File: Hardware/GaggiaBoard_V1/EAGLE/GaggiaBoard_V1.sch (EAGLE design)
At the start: 122 parts, among them IC1 LD117ADT33TR, J10 PIN262409-1, J11 PIN262409-1, J12 PIN262409-1, J13 PIN262409-1, J14 PIN262409-1, J15 PIN262409-1, J16 PIN262409-1, J17 PIN262409-1, J18 PIN262409-1, J19 PIN262409-1, J2 QWIIC_RIGHT_ANGLE, J20 PIN262409-1, J21 PIN262409-1, J22 PIN262409-1, J23 PIN262409-1, J24 5033981892, J3 QWIIC_RIGHT_ANGLE, J4 1X2-3.5MM, J5 1X2-3.5MM, K1 RELAY-SPDT-JZC-11F, K2 RELAY-SPDT-JZC-11F, K3 RELAY-SPDT-JZC-11F, Q1 600mA/40V, Q2 600mA/40V, Q3 600mA/40V, Q4 600mA/40V, Q5 600mA/40V, Q6 600mA/40V, Q8 600mA/40V, Q9 600mA/40V, U1 BLACKPILL, U2 MAX31855K, U3 MAX31855K

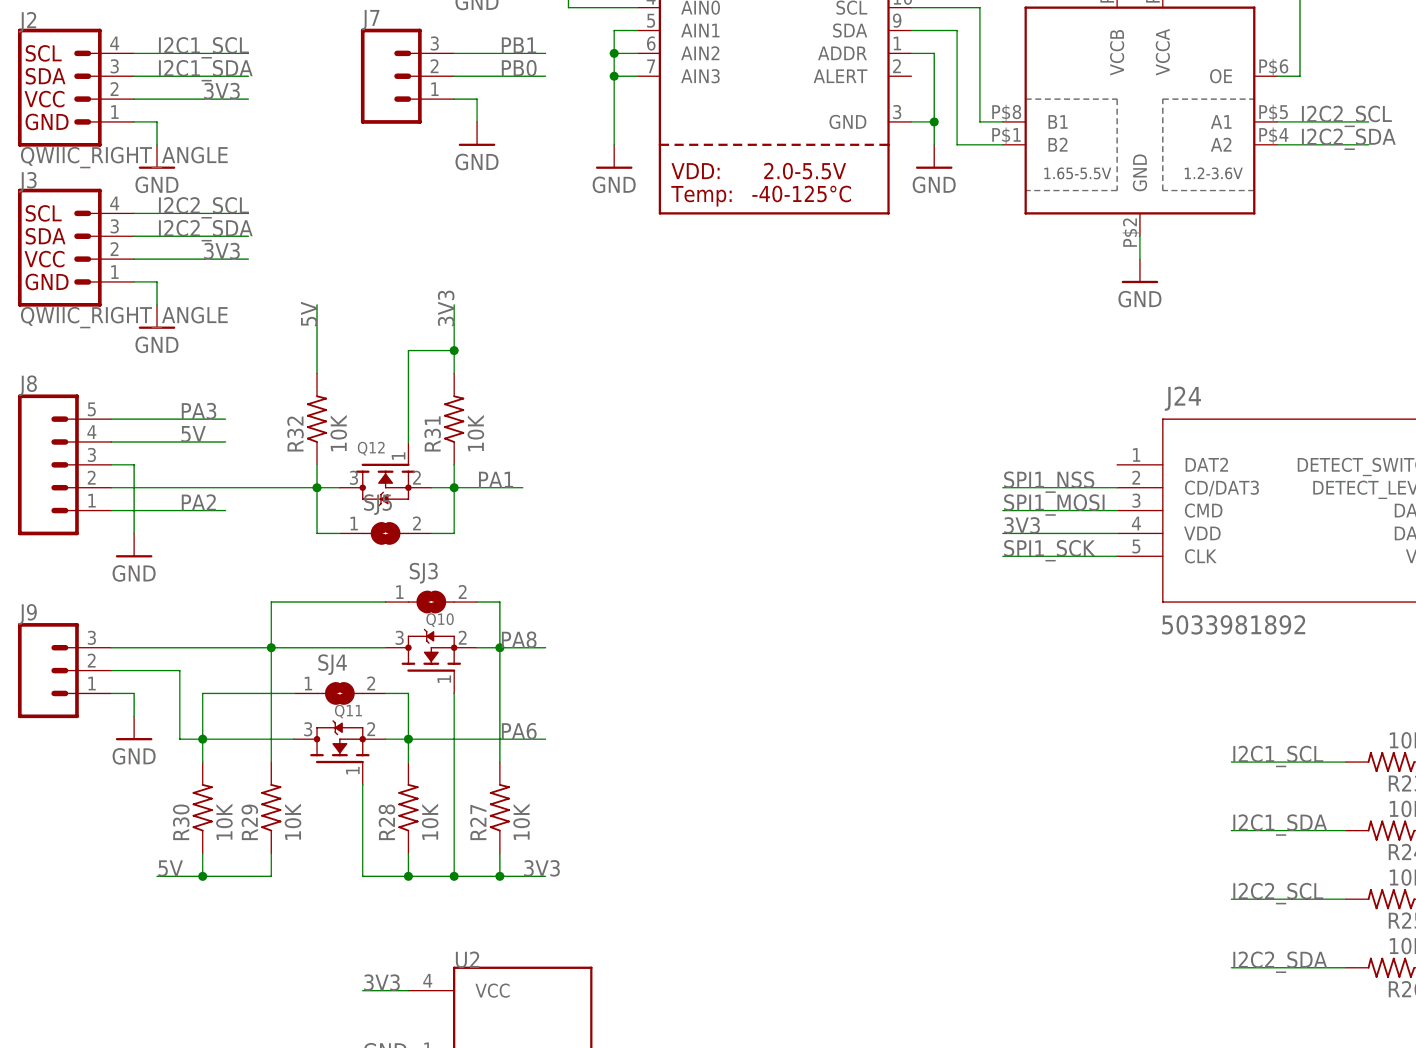
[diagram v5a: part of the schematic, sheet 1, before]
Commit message: TXU0102 level shifter for SSRs
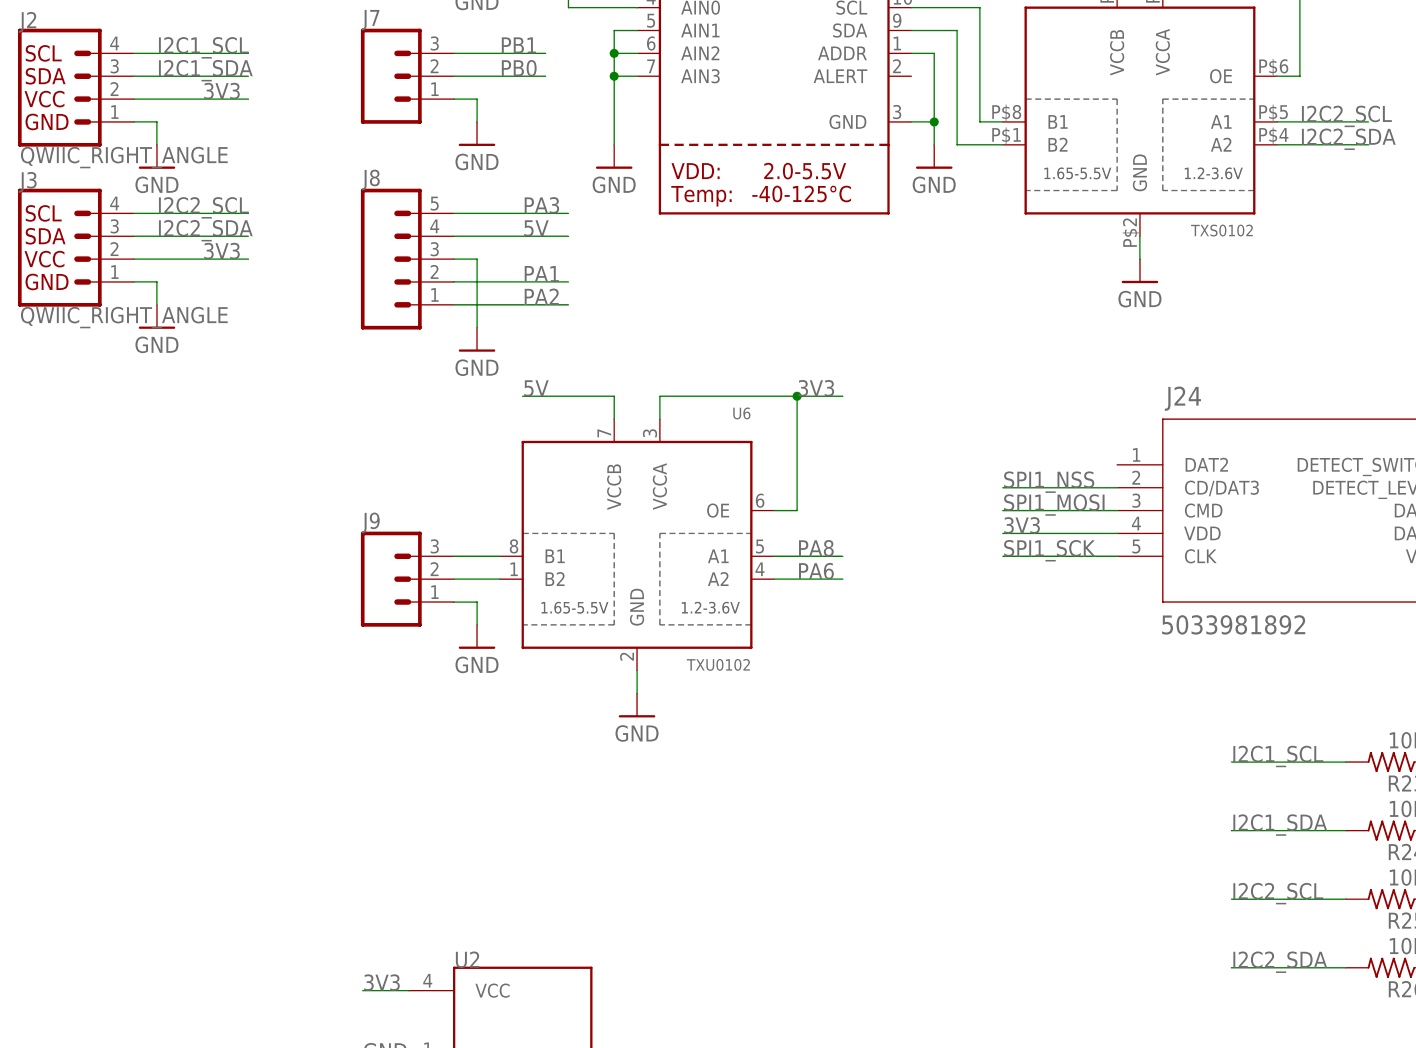
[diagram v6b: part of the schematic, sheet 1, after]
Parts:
- removed Q10, Q11, Q12: (no value), microbuilder:MOSFET-NREFLOW
- removed R27, R28, R29, R30, R31, R32: 10K, rcl:R-US_R0603
- removed SJ3, SJ4, SJ5: (no value), microbuilder:SOLDERJUMPER
- added U6: TXU0102, microbuilder:TXS0102
- U5: value (none) -> TXS0102
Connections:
- removed net N$43: J8.2, Q12.D, R32.1, SJ5.1
- net 3V3: now also U6.OE, U6.VCCA; no longer Q10.G, Q11.G, Q12.G, R27.1, R28.1, R31.2
- net 5V: now also U6.VCCB; no longer R29.1, R30.1, R32.2
- net GND: now also U6.GND
- net N$41: now also J9.3, U6.B1; no longer J9.2, Q11.D, R30.2, SJ4.1
- net N$42: now also J9.2, U6.B2; no longer J9.3, Q10.D, R29.2, SJ3.1
- net PA1: now also J8.2; no longer Q12.S, R31.1, SJ5.2
- net PA6: now also U6.A2; no longer Q11.S, R28.2, SJ4.2
- net PA8: now also U6.A1; no longer Q10.S, R27.2, SJ3.2
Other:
- moved on the sheet: J8, J9

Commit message: UARTs reassigned, LEDs fixed
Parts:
- added J27: (no value), SparkFun-Connectors:CONN_041X04_NO_SILK
- LED1, LED2, LED3, LED4: device led:LEDCHIP-LED0603 -> adafruit:LEDCHIPLED_1206
- R6: value 10k -> 10K
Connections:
- net UART1_5V_RX renamed UART6_5V_RX
- net UART1_5V_TX renamed UART6_5V_TX
- new net UART6_RX: Q7G$2.S, R18.1, SJ2.1, U1.PA12
- new net UART6_TX: Q7G$1.S, R19.1, SJ1.1, U1.PA11
- net 3V3: now also J27.1
- net GND: now also J27.4
- net UART1_RX: now also J27.3; no longer Q7G$2.S, R18.1, SJ2.1
- net UART1_TX: now also J27.2; no longer Q7G$1.S, R19.1, SJ1.1

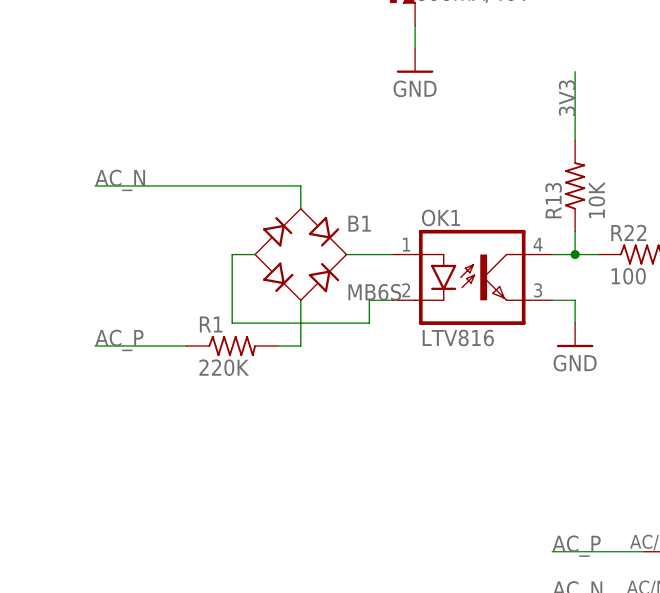
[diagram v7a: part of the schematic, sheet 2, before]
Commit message: Connectors spacing fixed
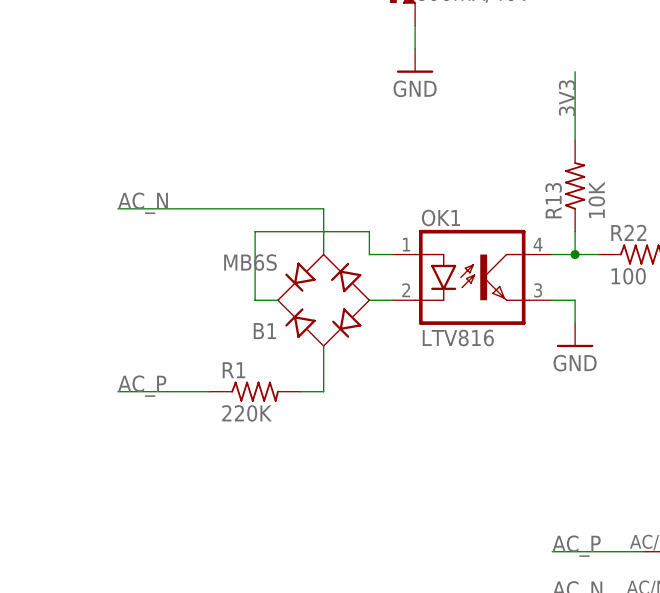
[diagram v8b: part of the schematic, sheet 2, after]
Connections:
- net AC_N: now also B1.AC2; no longer B1.AC1
- net N$37: now also B1.AC1; no longer B1.AC2
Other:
- moved on the sheet: B1, R1
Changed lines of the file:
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@@
 <attribute name="LCSC" x="50.8" y="68.58" size="1.778" layer="96" display="off"/>
 </instance>
-<instance part="R1" gate="G$1" x="22.86" y="60.96" smashed="yes">
-<attribute name="NAME" x="19.05" y="62.4586" size="1.778" layer="95"/>
-<attribute name="VALUE" x="19.05" y="57.658" size="1.778" layer="96"/>
-<attribute name="LCSC" x="22.86" y="60.96" size="1.778" layer="96" display="off"/>
+<instance part="R1" gate="G$1" x="25.4" y="55.88" smashed="yes">
+<attribute name="NAME" x="21.59" y="57.3786" size="1.778" layer="95"/>
+<attribute name="VALUE" x="21.59" y="52.578" size="1.778" layer="96"/>
+<attribute name="LCSC" x="25.4" y="55.88" size="1.778" layer="96" display="off"/>
 </instance>
 <instance part="SUPPLY8" gate="G$1" x="60.96" y="60.96" smashed="yes">
@@
 <attribute name="LCSC" x="60.96" y="78.74" size="1.778" layer="96" rot="R90" display="off"/>
 </instance>
-<instance part="B1" gate="G$1" x="30.48" y="71.12" smashed="yes">
-<attribute name="VALUE" x="35.56" y="66.04" size="1.778" layer="96"/>
-<attribute name="NAME" x="35.56" y="73.66" size="1.778" layer="95"/>
-<attribute name="LCSC" x="30.48" y="71.12" size="1.778" layer="96" display="off"/>
+<instance part="B1" gate="G$1" x="33.02" y="66.04" smashed="yes" rot="R180">
+<attribute name="VALUE" x="27.94" y="71.12" size="1.778" layer="96" rot="R180"/>
+<attribute name="NAME" x="27.94" y="63.5" size="1.778" layer="95" rot="R180"/>
+<attribute name="LCSC" x="33.02" y="66.04" size="1.778" layer="96" rot="R180" display="off"/>
 </instance>
 <instance part="R22" gate="G$1" x="68.58" y="71.12" smashed="yes">
@@
 </segment>
 <segment>
-<pinref part="B1" gate="G$1" pin="AC1"/>
-<wire x1="30.48" y1="76.2" x2="30.48" y2="78.74" width="0.1524" layer="91"/>
-<wire x1="30.48" y1="78.74" x2="7.62" y2="78.74" width="0.1524" layer="91"/>
-<label x="7.62" y="78.74" size="1.778" layer="95"/>
+<label x="10.16" y="76.2" size="1.778" layer="95"/>
+<pinref part="B1" gate="G$1" pin="AC2"/>
+<wire x1="33.02" y1="76.2" x2="10.16" y2="76.2" width="0.1524" layer="91"/>
+<wire x1="33.02" y1="71.12" x2="33.02" y2="76.2" width="0.1524" layer="91"/>
 </segment>
 <segment>
@@
 <segment>
 <pinref part="R1" gate="G$1" pin="1"/>
-<wire x1="17.78" y1="60.96" x2="7.62" y2="60.96" width="0.1524" layer="91"/>
-<label x="7.62" y="60.96" size="1.778" layer="95"/>
+<wire x1="20.32" y1="55.88" x2="10.16" y2="55.88" width="0.1524" layer="91"/>
+<label x="10.16" y="55.88" size="1.778" layer="95"/>
 </segment>
 <segment>
@@
 <pinref part="OK1" gate="G$1" pin="A"/>
 <pinref part="B1" gate="G$1" pin="+"/>
-<wire x1="40.64" y1="71.12" x2="35.56" y2="71.12" width="0.1524" layer="91"/>
+<wire x1="40.64" y1="71.12" x2="38.1" y2="71.12" width="0.1524" layer="91"/>
+<wire x1="25.4" y1="73.66" x2="38.1" y2="73.66" width="0.1524" layer="91"/>
+<wire x1="38.1" y1="73.66" x2="38.1" y2="71.12" width="0.1524" layer="91"/>
+<wire x1="27.94" y1="66.04" x2="25.4" y2="66.04" width="0.1524" layer="91"/>
+<wire x1="25.4" y1="66.04" x2="25.4" y2="73.66" width="0.1524" layer="91"/>
 </segment>
 </net>
@@
 <segment>
 <pinref part="B1" gate="G$1" pin="-"/>
-<wire x1="25.4" y1="71.12" x2="22.86" y2="71.12" width="0.1524" layer="91"/>
-<wire x1="22.86" y1="71.12" x2="22.86" y2="63.5" width="0.1524" layer="91"/>
-<wire x1="22.86" y1="63.5" x2="38.1" y2="63.5" width="0.1524" layer="91"/>
-<wire x1="38.1" y1="63.5" x2="38.1" y2="66.04" width="0.1524" layer="91"/>
 <pinref part="OK1" gate="G$1" pin="C"/>
 <wire x1="38.1" y1="66.04" x2="40.64" y2="66.04" width="0.1524" layer="91"/>
@@
 <segment>
 <pinref part="R1" gate="G$1" pin="2"/>
-<pinref part="B1" gate="G$1" pin="AC2"/>
-<wire x1="27.94" y1="60.96" x2="30.48" y2="60.96" width="0.1524" layer="91"/>
-<wire x1="30.48" y1="60.96" x2="30.48" y2="66.04" width="0.1524" layer="91"/>
-</segment>
-</net>
+<wire x1="33.02" y1="60.96" x2="33.02" y2="55.88" width="0.1524" layer="91"/>
+<pinref part="B1" gate="G$1" pin="AC1"/>
+<wire x1="30.48" y1="55.88" x2="33.02" y2="55.88" width="0.1524" layer="91"/>
+</segment>
+</net>
